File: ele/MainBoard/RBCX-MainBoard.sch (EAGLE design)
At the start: 278 parts, among them IC1 DRV8833PWP, IC10 INA180A4, IC2 INA180A4, IC3 INA180A4, IC4 DRV8833PWP, IC5 INA180A4, IC6 INA180A4, IC7 INA180A4, IC8 INA180A4, IC9 INA180A4, Q1 CHOOSE_ME, Q3 CHOOSE_ME, Q6 CHOOSE_ME, Q8 CHOOSE_ME, Q9 CHOOSE_ME, U1 STM32F103VCT6, X0 POWER_IN, X1 M3B, X2 M4B, X3 M3B, X4 M4B, X5 POWER_OUT, Y1 3215_2P, Y2 5032/2P

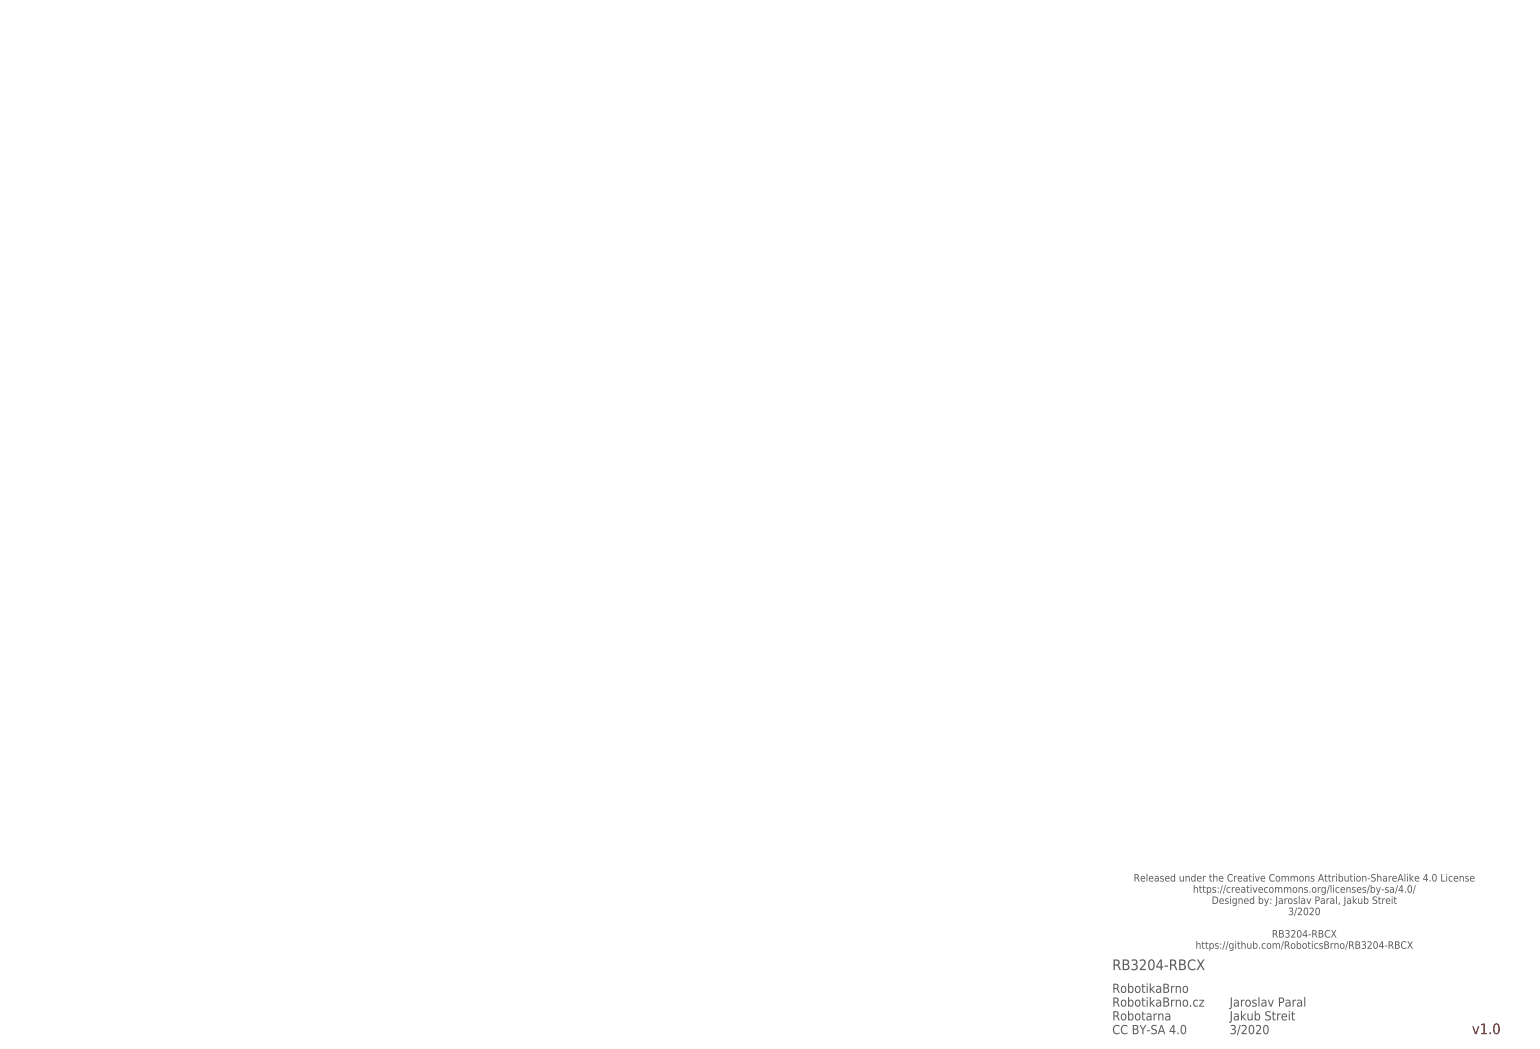
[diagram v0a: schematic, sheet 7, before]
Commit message: MainBoardSCH: Add ESP connectors
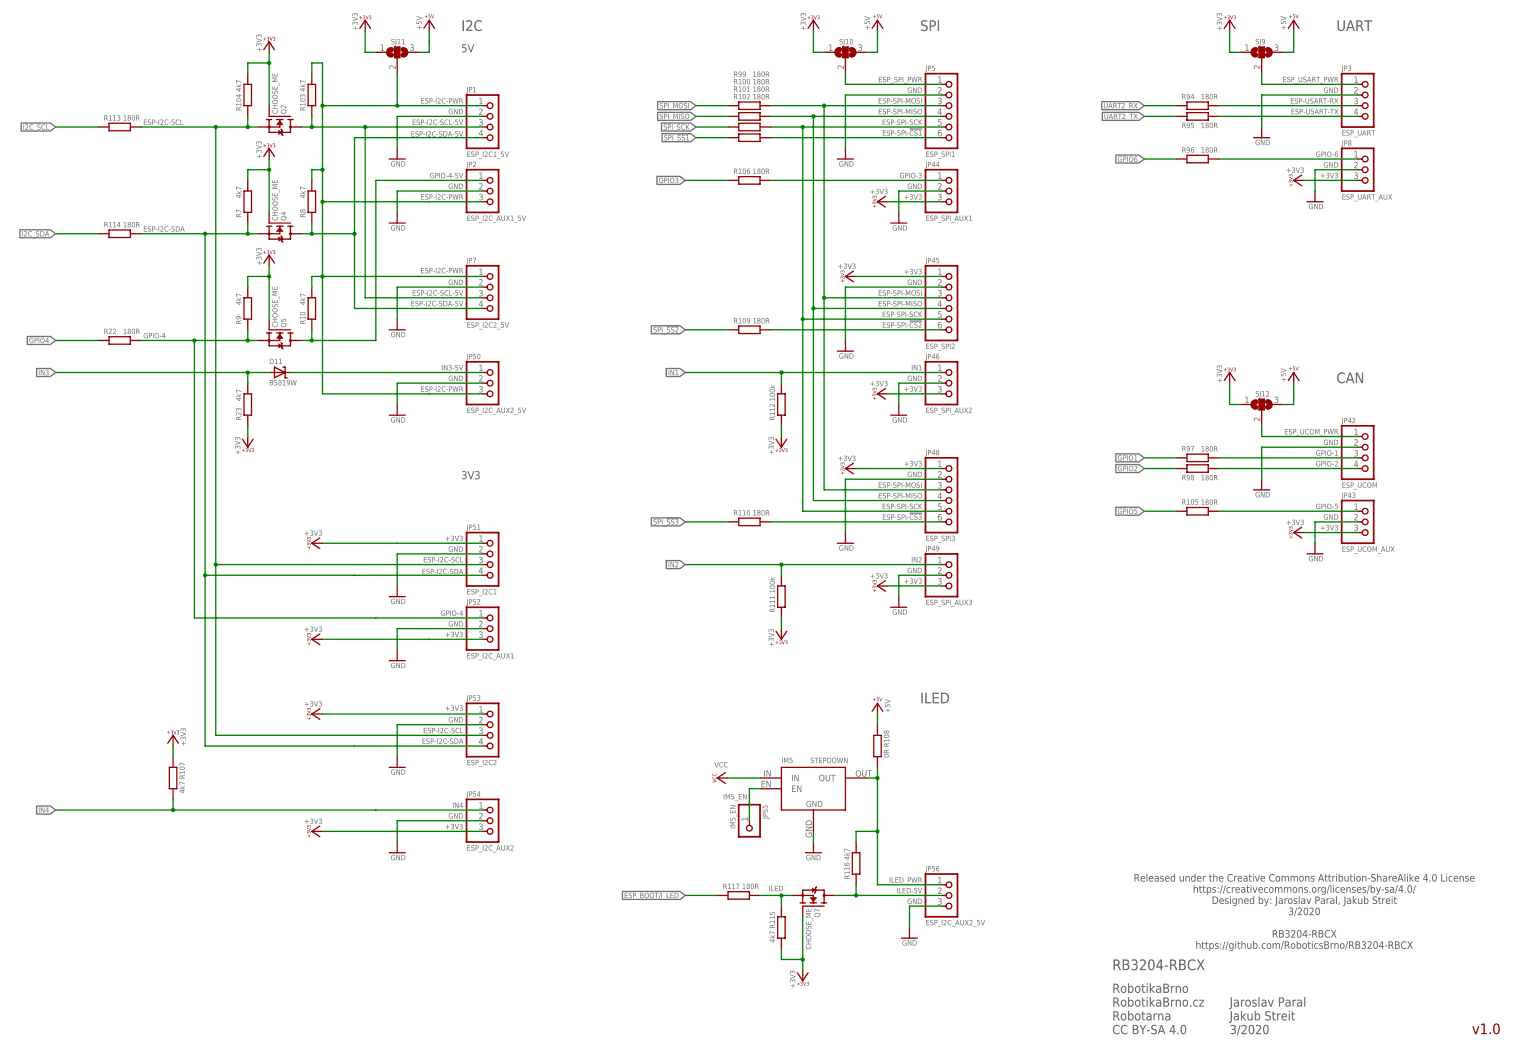
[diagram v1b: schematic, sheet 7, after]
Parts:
- removed SJ8: (no value), jumper:SJ2W
- added D11: B5819W, diode:SHOTTKY-SOD123
- added IM5: STEPDOWN, StepDown:STEPDOWN
- added JP42: ESP_UCOM, pinhead:PINHD-1X4
- added JP43: ESP_UCOM_AUX, pinhead:PINHD-1X3
- added JP44: ESP_SPI_AUX1, pinhead:PINHD-1X3
- added JP45: ESP_SPI2, pinhead:PINHD-1X6
- added JP46: ESP_SPI_AUX2, pinhead:PINHD-1X3
- added JP48: ESP_SPI3, pinhead:PINHD-1X6
- added JP49: ESP_SPI_AUX3, pinhead:PINHD-1X3
- added JP50, JP56: ESP_I2C_AUX2_5V, pinhead:PINHD-1X3
- added JP51: ESP_I2C1, pinhead:PINHD-1X4
- added JP52: ESP_I2C_AUX1, pinhead:PINHD-1X3
- added JP53: ESP_I2C2, pinhead:PINHD-1X4
- added JP54: ESP_I2C_AUX2, pinhead:PINHD-1X3
- added JP55: IM5_EN, pinhead:PINHD-1X1
- added JP8: ESP_UART_AUX, pinhead:PINHD-1X3
- added Q2, Q4, Q5, Q7: CHOOSE_ME, transistors:N-MOSFET-SOT323-GSD
- added R105, R106, R109, R110, R113, R114, R117, R118, R119, R120, R121, R97, R98: 180R, rcl_upravena:R-EU_R0603
- added R107, R115, R116: 4k7, rcl_upravena:R-EU_R0603
- added R108: 0R, rcl_upravena:R-EU_R1206S
- added R111, R112: 100k, rcl_upravena:R-EU_R0603
- added SJ12: (no value), jumper:SJ2W
- JP1: value ESP-I2C-CAN-UART -> ESP_I2C1_5V
- JP2: value ESP_I2C -> ESP_I2C_AUX1_5V; device pinhead:PINHD-1X4 -> pinhead:PINHD-1X3
- JP3: value ESP_USART -> ESP_UART; device pinhead:PINHD-1X7 -> pinhead:PINHD-1X4
- JP5: value ESP_SPI -> ESP_SPI1
- JP7: value STM_ANALOG -> ESP_I2C2_5V
- R10, R103, R104, R7, R8, R9: value 180R -> 4k7
- R22: value 4k7 -> 180R
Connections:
- net ESP-SPI-!CS renamed ESP-SPI-!CS1
- net ESP_USART_PWR1 renamed ESP_SPI_PWR
- removed net DAC1: IM6.IO25
- removed net DAC2: IM6.IO26
- removed net ESP-I2C-SCL-CAN-UART-RX: JP1.3, R7.2
- removed net ESP-I2C-SDA-CAN-UART-TX: JP1.4, R8.2
- removed net ESP-USART-DIR: JP3.5, R96.2
- removed net ESP_I2C_PWR: JP2.1, R22.2, R23.2, SJ8.2
- removed net GPIO0: IM6.IO32
- removed net I_LED: IM6.IO15
- removed net N$10: R94.1
- removed net N$12: R95.1
- removed net UART_AUX: IM6.IO27
- new net ESP-I2C-PWR: JP1.1, JP2.3, JP50.3, JP7.1, R10.2, R103.2, R8.2, SJ11.2
- new net ESP-I2C-SCL-5V: JP1.3, JP7.3, Q2.D, R103.1
- new net ESP-I2C-SDA-5V: JP1.4, JP7.4, Q4.D, R8.1
- new net ESP-SPI-!CS2: JP45.6, R109.2
- new net ESP-SPI-!CS3: JP48.6, R110.2
- new net ESP_BOOT/I_LED: IM6.IO0, R117.1, R6.1
- new net ESP_UCOM_PWR: JP42.1, SJ12.2
- new net GPIO-1: JP42.3, R97.2
- new net GPIO-2: JP42.4, R98.2
- new net GPIO-3: JP44.1, R106.2
- new net GPIO-4: JP52.1, Q5.S, R22.2, R9.1
- new net GPIO-4-5V: JP2.1, Q5.D, R10.1
- new net GPIO-5: JP43.1, R105.2
- new net GPIO-6: JP8.1, R96.2
- new net GPIO2: IM6.IO33, R98.1
- new net GPIO3: IM6.IO25, R106.1
- new net GPIO4: IM6.IO26, R22.1
- new net GPIO5: IM6.IO27, R105.1
- new net GPIO6: IM6.IO4, R96.1
- new net ILED: Q7.S, R115.1, R117.2
- new net ILED-5V: JP56.2, Q7.D, R116.1
- new net ILED_PWR: IM5.OUT, JP56.1, R108.2, R116.2
- new net IM5_EN: IM5.EN, JP55.1
- new net IN3-5V: D11.C, JP50.1
- net +3V3: now also JP43.3, JP44.3, JP45.1, JP46.3, JP48.1, JP49.3, JP51.1, JP52.3, JP53.1, JP54.3, JP8.3, Q2.G, Q4.G, Q5.G, Q7.G, R104.2, R107.1, R111.1, R112.1, R115.2, R23.1, R7.2, R9.2, SJ11.1, SJ12.1; no longer SJ8.1
- net +3V3S: no longer SJ11.1
- net +5V: now also R108.1, SJ12.3; no longer JP1.1, SJ8.3
- net ESP-I2C-SCL: now also JP51.3, JP53.3, Q2.S, R104.1, R113.2; no longer JP2.3, R10.2, R22.1
- net ESP-I2C-SDA: now also JP51.4, JP53.4, Q4.S, R114.2, R7.1; no longer JP2.4, R23.1, R9.2
- net ESP-SPI-MISO: now also JP45.4, JP48.4
- net ESP-SPI-MOSI: now also JP45.3, JP48.3
- net ESP-SPI-SCK: now also JP45.5, JP48.5
- net ESP_BOOT: now also R6.2; no longer IM6.IO0
- net ESP_COM_RX: now also R118.2
- net ESP_COM_TX: now also R119.2
- net ESP_PROG_RX: now also R120.2
- net ESP_PROG_TX: now also R121.2
- net EXPANDER_RX: now also R119.1
- net EXPANDER_TX: now also R118.1
- net GND: now also IM5.GND, JP42.2, JP43.2, JP44.2, JP45.2, JP46.2, JP48.2, JP49.2, JP50.2, JP51.2, JP52.2, JP53.2, JP54.2, JP56.3, JP8.2
- net GPIO1: now also IM6.IO32, R97.1; no longer IM6.IO33
- net I2C_SCL: now also R113.1; no longer R9.1
- net I2C_SDA: now also R114.1; no longer R10.1
- net IN1: now also IM6.SVP, JP46.1, R112.2; no longer IM6.IO35
- net IN2: now also IM6.SVN, JP49.1, R111.2; no longer IM6.IO34
- net IN3: now also D11.A, IM6.IO34, R23.2; no longer IM6.SVN
- net IN4: now also IM6.IO35, JP54.1, R107.2; no longer IM6.SVP
- net INTELLIGENT_SERVO: now also IM6.IO14; no longer IM6.IO4
- net SPI_!SS1: now also R102.1
- net SPI_!SS2: now also IM6.IO15, R109.1; no longer IM6.IO13
- net SPI_!SS3: now also IM6.IO13, R110.1; no longer IM6.IO14
- net SPI_SCK: no longer R102.1
- net STM-AIO-POWER: no longer JP7.1, SJ11.2
- net STM-AIO1: no longer JP7.3, R104.2
- net STM-AIO2: no longer JP7.4, R103.2
- net UART2_RX: now also R94.1
- net UART2_TX: now also R95.1
- net UART_RX: now also R121.1
- net UART_TX: now also R120.1
- net VCC: now also IM5.IN
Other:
- note added: "3V3"
- note added: "5V"
- note added: "CAN"
- note added: "I2C"
- note added: "ILED"
- note added: "SPI"
- note added: "UART"
- moved on the sheet: R6

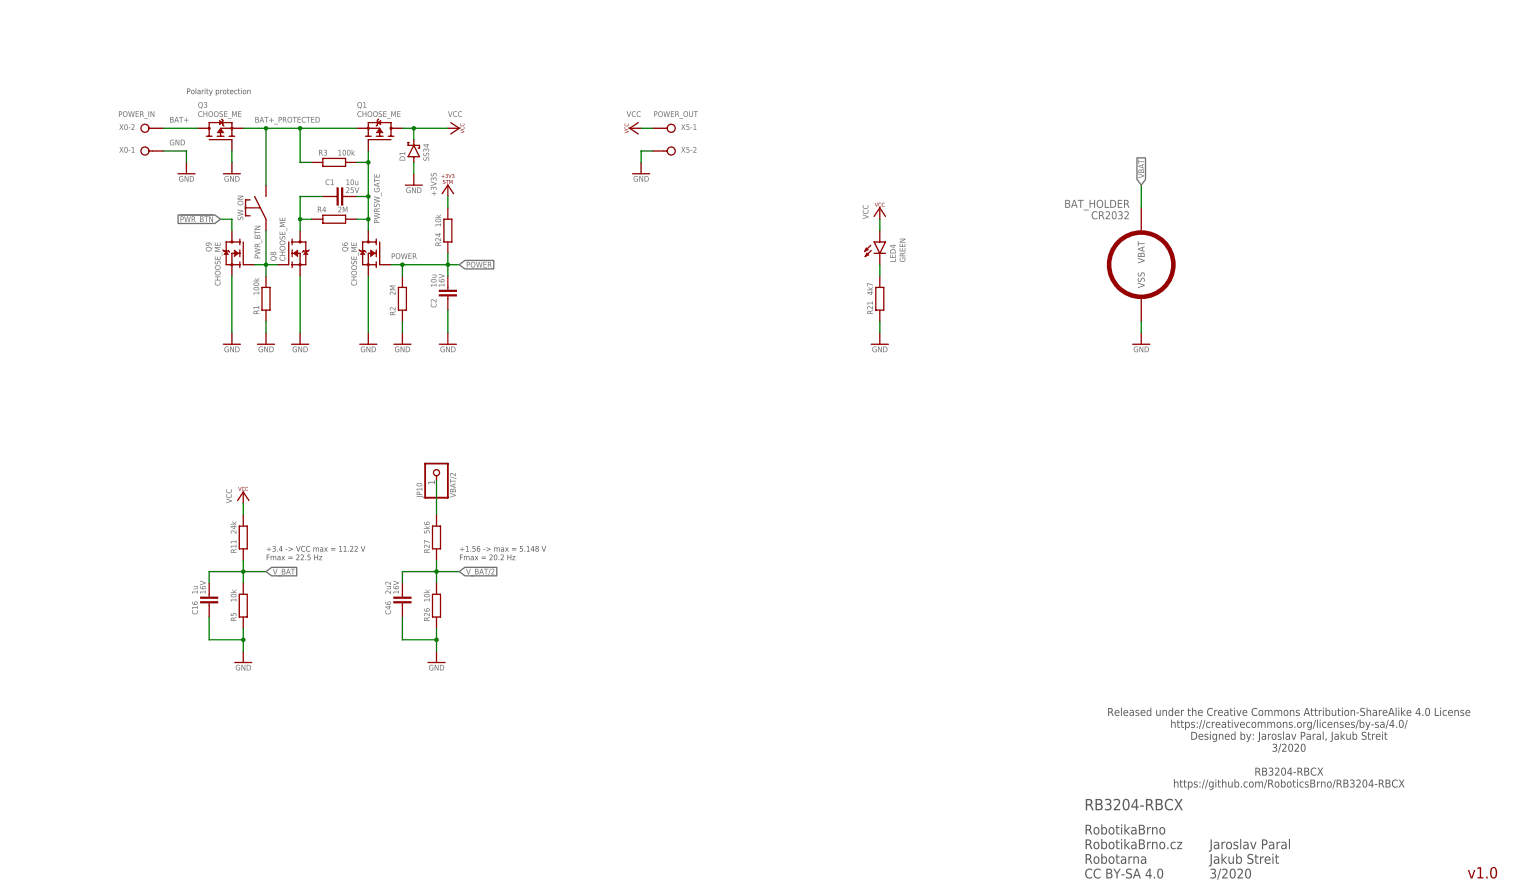
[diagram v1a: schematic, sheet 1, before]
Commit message: MainBoardSCH: Add main voltage regulators and power LEDs
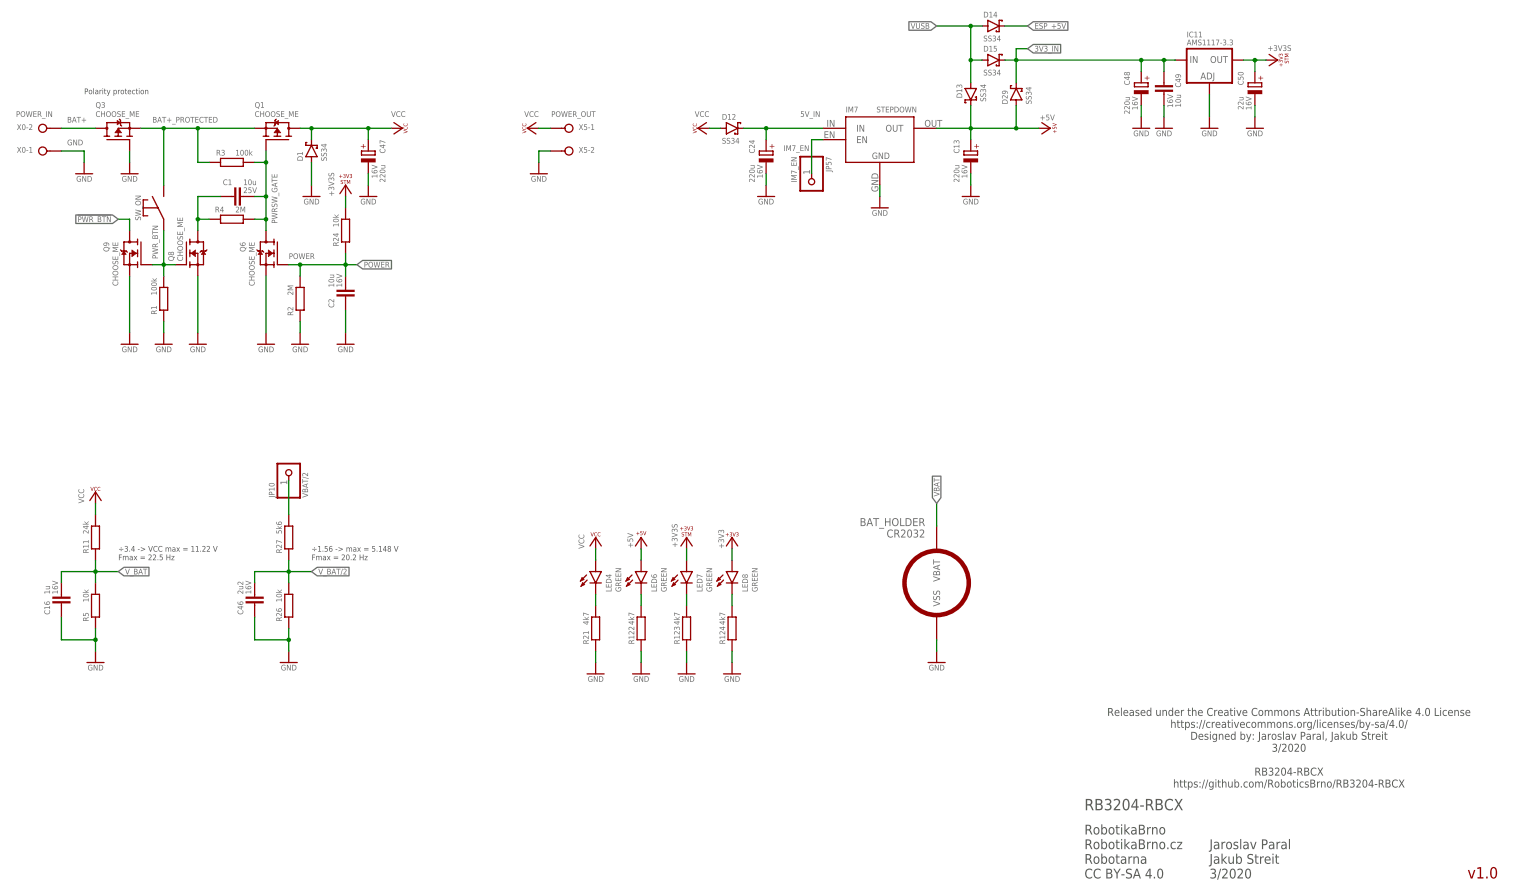
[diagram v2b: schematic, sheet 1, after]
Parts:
- added C13, C14, C24, C47, C48: 220u, rcl_upravena:CPOL-EU153CLV-1010
- added C22, C49: 10u, rcl_upravena:C-EUC0805
- added C50: 22u, rcl_upravena:CPOL-EUB/3528-21R
- added D12, D13, D14, D15, D29: SS34, diode:BAT60JDO-214-AB
- added IC11: AMS1117-3.3, v-reg:LM317MSTT3
- added IM7: STEPDOWN, StepDown:STEPDOWN
- added JP57: IM7_EN, pinhead:PINHD-1X1
- added LED6, LED7, LED8: GREEN, led:LEDSML0603
- added R122, R123, R124: 4k7, rcl_upravena:R-EU_R0603
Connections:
- new net 3V3_IN: C48.+, C49.2, D15.C, D29.C, IC11.IN
- new net 5V_IN: C24.+, D12.C, IM7.IN
- new net IM7_EN: IM7.EN, JP57.1
- new net PWRLED_VCC1: LED6.C, R122.2
- new net PWRLED_VCC2: LED7.C, R123.2
- new net PWRLED_VCC3: LED8.C, R124.2
- net +3V3: now also LED8.A
- net +3V3S: now also C50.+, IC11.OUT, LED7.A
- net +5V: now also C13.+, D13.C, D29.A, IM7.OUT, LED6.A
- net ESP_+5V: now also C14.+, C22.2, D14.C
- net GND: now also C13.-, C14.-, C22.1, C24.-, C47.-, C48.-, C49.1, C50.-, IC11.ADJ, IM7.GND, R122.1, R123.1, R124.1
- net VCC: now also C47.+, D12.A
- net VUSB: now also D13.A, D14.A, D15.A
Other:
- moved on the sheet: BAT_HOLDER, C1, C16, C2, C46, D1, D2, JP10, LED4, Q1, Q3, Q6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
